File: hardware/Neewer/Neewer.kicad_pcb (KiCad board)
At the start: 2 copper layers, 83.8 x 99.1 mm, 31 parts, among them J1 Screw_Terminal_01x03, J2 Screw_Terminal_01x03, J3 PSU, Q1 IRLZ44N, Q2 IRLZ44N, Q3 IRLZ44N, Q4 IRLZ44N

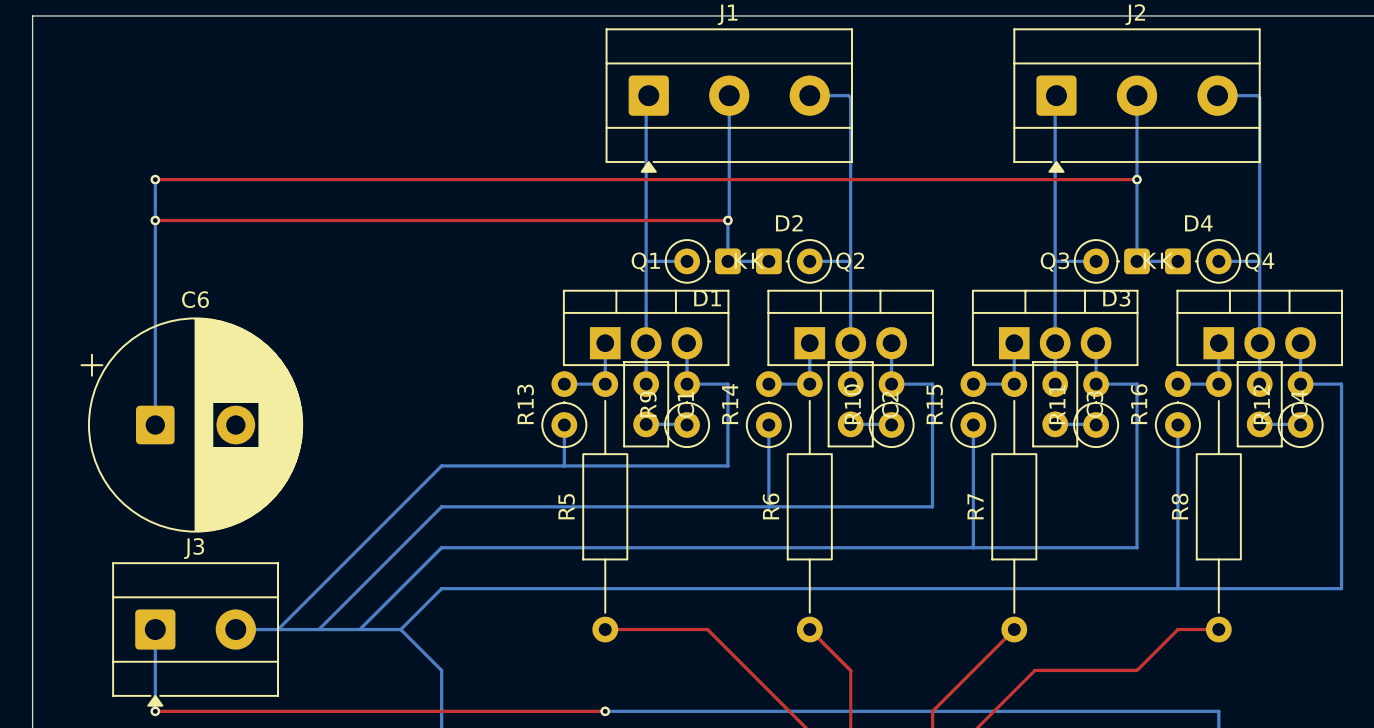
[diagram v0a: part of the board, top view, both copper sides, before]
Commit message: Update kicad
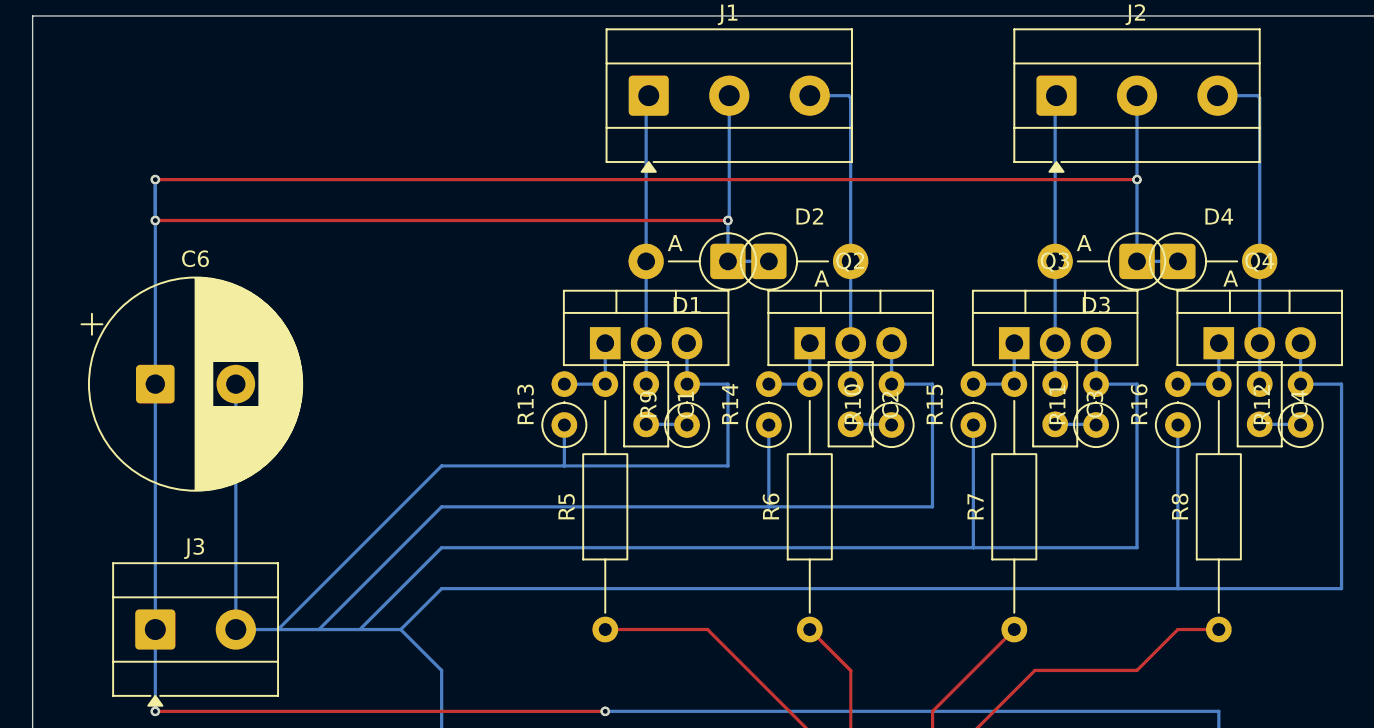
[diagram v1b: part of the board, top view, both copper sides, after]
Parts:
- D1, D2, D3, D4: value BAT46 -> 1N5819; footprint Diode_THT:D_DO-35_SOD27_P2.54mm_Vertical_KathodeUp -> Diode_THT:D_DO-41_SOD81_P5.08mm_Vertical_AnodeUp
- moved C6 2.54 mm to (50.8, 61.0)
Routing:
- net VCC: track 211.1 -> 226.4 mm
- net GND: track 333.8 -> 349.1 mm
- net PWM2: track 22.9 -> 20.4 mm
- net PWM4: track 23.0 -> 20.5 mm
- net PWM3: track 20.5 -> 17.9 mm
- net PWM1: track 20.5 -> 18.0 mm
